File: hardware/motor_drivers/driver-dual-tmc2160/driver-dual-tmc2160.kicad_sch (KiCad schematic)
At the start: 76 parts, among them M1 Micro-Fit 3.0, M2 Micro-Fit 3.0, Q1 DMHT6016LFJ, Q2 DMHT6016LFJ, Q3 DMHT6016LFJ, Q4 DMHT6016LFJ, T1 GND, T10 SCK, T11 GND, T12 DIR, T13 ENCB, T14 SDI, T15 EN, T16 ENCN, T17 SDO, T18 VCC, T19 SPI_MODE, T2 CS0, T20 SD_MODE, T21 Therm, T3 DIAG0, T4 CLK, T5 STEP, T6 DIAG1, T7 12V, T8 GND, T9 ENCA, U1 TMC2160, U2 TMC2160

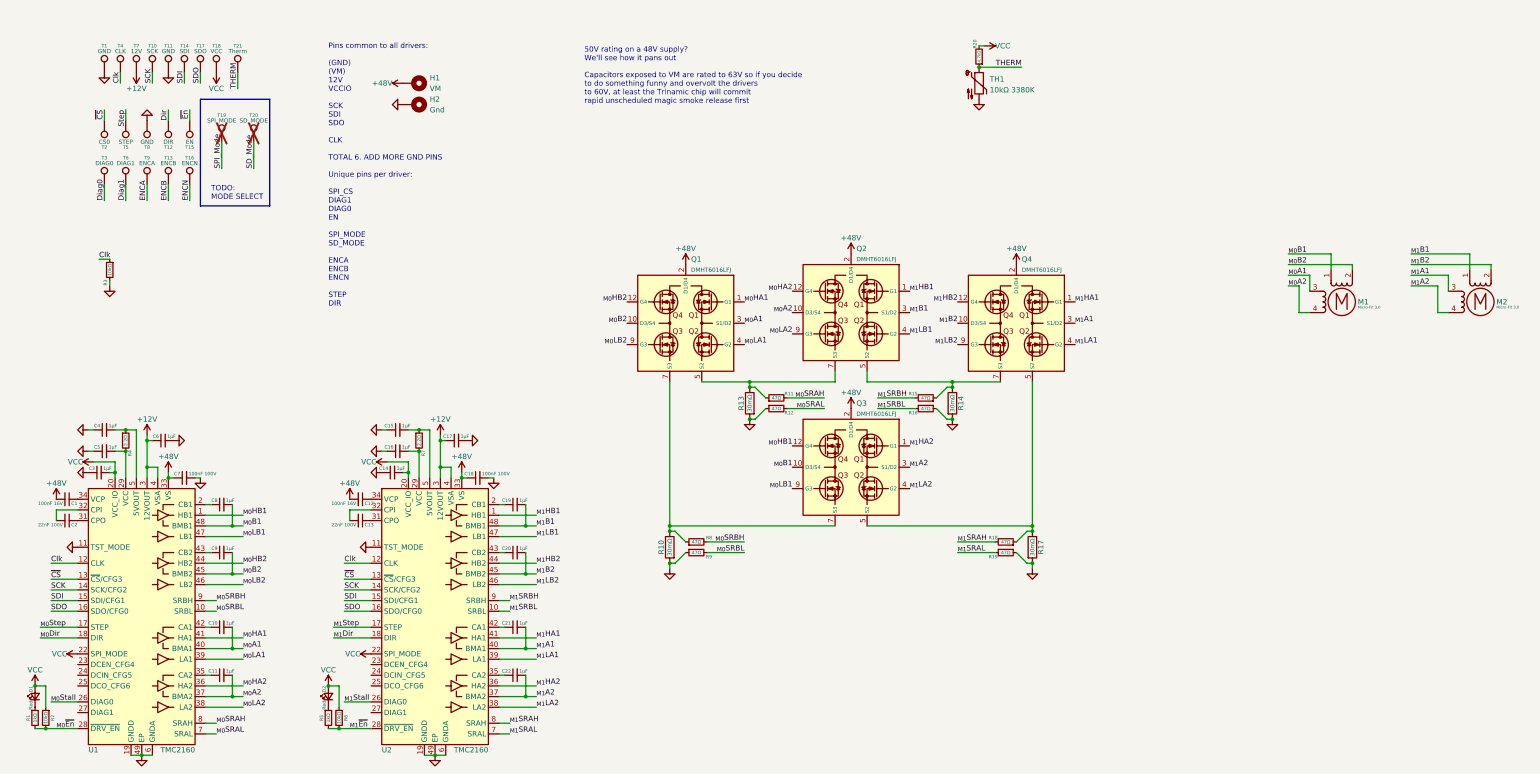
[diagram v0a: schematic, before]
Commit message: added ctb v0.3 and dual 2160, fixed typo in v0.6 manual
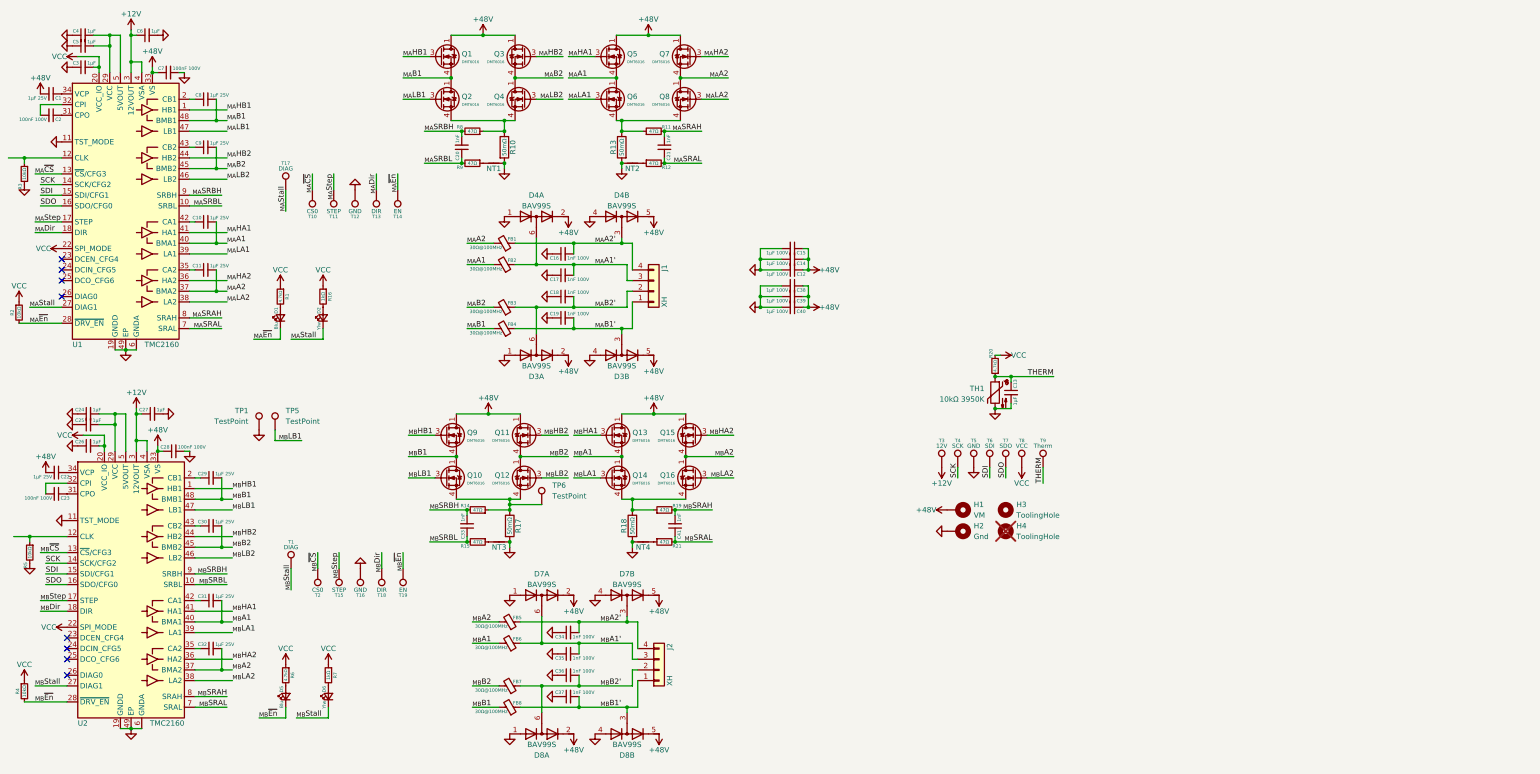
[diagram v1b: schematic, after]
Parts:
- removed M2: Micro-Fit 3.0, corevus:XKB_X3025WR-04, symbol Motor:Stepper_Motor_bipolar
- removed Q1, Q2, Q3, Q4: DMHT6016LFJ, corevus:V-DFN5045-12-Type-B, symbol corevus:DMHT6016LFJ
- removed R14: 30mΩ, Resistor_SMD:R_1206_3216Metric, symbol Device:R
- removed R18: 47Ω, AlphaLib:0402R, symbol Device:R_Small
- removed T13: ENCB, corevus:LGA_Land, symbol Connector:TestPoint
- removed T20: SD_MODE, corevus:LGA_Land, symbol Connector:TestPoint
- removed T4: CLK, corevus:LGA_Land, symbol Connector:TestPoint
- removed T6: DIAG1, corevus:LGA_Land, symbol Connector:TestPoint
- removed T9: ENCA, corevus:LGA_Land, symbol Connector:TestPoint
- added C23, C28: 100nF 100V, PCM_ME_passives:0402C, symbol Device:C_Small
- added C24, C27: 1μF, PCM_ME_passives:0402C, symbol Device:C_Small
- added C25, C26: 1µF, PCM_ME_passives:0402C, symbol Device:C_Small
- added C29, C30, C31, C32: 1μF 25V, PCM_ME_passives:0402C, symbol Device:C_Small
- added C33, C41: 1nF, PCM_ME_passives:0402C, symbol Device:C_Small
- added C34, C35, C36, C37: 1nF 100V, PCM_ME_passives:0402C, symbol Device:C_Small
- added C38, C39, C40: 1μF 100V, Capacitor_SMD:C_1206_3216Metric, symbol Device:C_Small
- added D3, D4, D7, D8: BAV99S, Package_TO_SOT_SMD:SOT-363_SC-70-6, symbol Diode:BAV99S
- added D5: Blu, PCM_ME_passives:0402LED, symbol Device:LED_Small
- added D6: Ylw, PCM_ME_passives:0402LED, symbol Device:LED_Small
- added FB1, FB2, FB3, FB4, FB5, FB6, FB7, FB8: 30Ω@100MHz, Resistor_SMD:R_1206_3216Metric, symbol Device:FerriteBead_Small
- added H3, H4: ToolingHole, corevus:ToolingHole, symbol Mechanical:MountingHole
- added J2: XH, corevus:JST_XH_1x04, symbol Connector_Generic:Conn_01x04
- added NT1, NT2, NT3, NT4: NetTie_2, corevus:NetTie-2_SMD_Pad0.1mm, symbol Device:NetTie_2
- added Q1, Q10, Q11, Q12, Q13, Q14, Q15, Q16, Q2, Q3, Q4, Q5, Q6, Q7, Q8, Q9: DMT6016, corevus:DMT6016LFDF, symbol corevus:DMT6016LFDF-7
- added R14, R21: 47Ω, PCM_ME_passives:0402R, symbol Device:R_Small
- added R18: 50mΩ, Resistor_SMD:R_1206_3216Metric, symbol Device:R
- added T15: STEP, corevus:LGA_Land_2.5mm, symbol Connector:TestPoint
- added T18: DIR, corevus:LGA_Land_2.5mm, symbol Connector:TestPoint
- added T2: CS0, corevus:LGA_Land_2.5mm, symbol Connector:TestPoint
- added TP1, TP5, TP6: TestPoint, TestPoint:TestPoint_Pad_D1.0mm, symbol Connector:TestPoint
- C1: value 100nF 16V -> 1μF 25V; footprint AlphaLib:0402C -> PCM_ME_passives:0402C
- C10, C11, C22, C8, C9: value 1μF -> 1μF 25V; footprint AlphaLib:0402C -> PCM_ME_passives:0402C
- C12: value 100nF 16V -> 1μF 100V; footprint AlphaLib:0402C -> Capacitor_SMD:C_1206_3216Metric
- C13: value 22nF 100V -> 1μF; footprint AlphaLib:0402C -> PCM_ME_passives:0402C
- C14: value 1µF -> 1μF 100V; footprint AlphaLib:0402C -> Capacitor_SMD:C_1206_3216Metric
- C15: value 1μF -> 1μF 100V; footprint AlphaLib:0402C -> Capacitor_SMD:C_1206_3216Metric
- C16: value 1µF -> 1nF 100V; footprint AlphaLib:0402C -> PCM_ME_passives:0402C
- C17, C19: value 1μF -> 1nF 100V; footprint AlphaLib:0402C -> PCM_ME_passives:0402C
- C18: value 100nF 100V -> 1nF 100V; footprint AlphaLib:0402C -> PCM_ME_passives:0402C
- C2: value 22nF 100V -> 100nF 100V; footprint AlphaLib:0402C -> PCM_ME_passives:0402C
- C20, C21: value 1μF -> 1nF; footprint AlphaLib:0402C -> PCM_ME_passives:0402C
- C3, C4, C5, C6, C7: footprint AlphaLib:0402C -> PCM_ME_passives:0402C
- D1: value Red -> Blu; footprint AlphaLib:0603LED -> PCM_ME_passives:0402LED
- D2: value Red -> Ylw; footprint AlphaLib:0603LED -> PCM_ME_passives:0402LED
- H1, H2: now left out of the parts list
- J1: renamed from M1; value Micro-Fit 3.0 -> XH; footprint corevus:XKB_X3025WR-04 -> corevus:JST_XH_1x04; symbol Motor:Stepper_Motor_bipolar -> Connector_Generic:Conn_01x04
- R1: value 1kΩ -> 4.7kΩ; footprint AlphaLib:0402R -> PCM_ME_passives:0402R
- R10, R13, R17: value 30mΩ -> 50mΩ
- R11, R12, R15, R19, R2, R20, R3, R8, R9: footprint AlphaLib:0402R -> PCM_ME_passives:0402R
- R16: value 47Ω -> 1kΩ; footprint AlphaLib:0402R -> PCM_ME_passives:0402R
- R4: value 2.2Ω -> 10kΩ; footprint AlphaLib:0402R -> PCM_ME_passives:0402R
- R5: value 1kΩ -> 10kΩ; footprint AlphaLib:0402R -> PCM_ME_passives:0402R
- R6: value 10kΩ -> 4.7kΩ; footprint AlphaLib:0402R -> PCM_ME_passives:0402R
- R7: value 2.2Ω -> 1kΩ; footprint AlphaLib:0402R -> PCM_ME_passives:0402R
- T1: value GND -> DIAG; footprint corevus:LGA_Land -> corevus:LGA_Land_2.5mm
- T10: renamed from T2; footprint corevus:LGA_Land -> corevus:LGA_Land_2.5mm
- T11: renamed from T5; footprint corevus:LGA_Land -> corevus:LGA_Land_2.5mm
- T12: renamed from T8; footprint corevus:LGA_Land -> corevus:LGA_Land_2.5mm
- T13: renamed from T12; footprint corevus:LGA_Land -> corevus:LGA_Land_2.5mm
- T14: renamed from T15; footprint corevus:LGA_Land -> corevus:LGA_Land_2.5mm
- T16: value ENCN -> GND; footprint corevus:LGA_Land -> corevus:LGA_Land_2.5mm
- T17: renamed from T3; value DIAG0 -> DIAG; footprint corevus:LGA_Land -> corevus:LGA_Land_2.5mm
- T19: value SPI_MODE -> EN; footprint corevus:LGA_Land -> corevus:LGA_Land_2.5mm; now fitted
- T3: renamed from T7; footprint corevus:LGA_Land -> corevus:LGA_Land_2.5mm
- T4: renamed from T10; footprint corevus:LGA_Land -> corevus:LGA_Land_2.5mm
- T5: renamed from T11; footprint corevus:LGA_Land -> corevus:LGA_Land_2.5mm
- T6: renamed from T14; footprint corevus:LGA_Land -> corevus:LGA_Land_2.5mm
- T7: renamed from T17; footprint corevus:LGA_Land -> corevus:LGA_Land_2.5mm
- T8: renamed from T18; footprint corevus:LGA_Land -> corevus:LGA_Land_2.5mm
- T9: renamed from T21; footprint corevus:LGA_Land -> corevus:LGA_Land_2.5mm
- TH1: value 10kΩ 3380K -> 10kΩ 3950K; footprint AlphaLib:0402R -> PCM_ME_passives:0402R
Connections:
- net Diag0 is gone; now on net _{MA}Stall: T17.1
- net ENCN is gone; now on net GND: T16.1
- net _{M0}Dir is gone; now on net _{MA}Dir: U1.18 (DIR)
- net _{M0}Step is gone; now on net _{MA}Step: U1.17 (STEP)
- net ~{En} is gone; now on net _{MA}~{En}: T14.1
- net +12V: now also C27.1; no longer C17.1
- net +48V: now also C12.1, C14.1, C15.1, C22.2, C28.1, C38.1, C39.1, C40.1, D3.2 (K2), D3.5 (K4), D4.2 (K2), D4.5 (K4), D7.2 (K2), D7.5 (K4), D8.2 (K2), D8.5 (K4), Q1.1 (D), Q1.2 (D), Q1.5 (D), Q1.6 (D), Q1.8 (D), Q11.1 (D), Q11.2 (D), Q11.5 (D), Q11.6 (D), Q11.8 (D), Q13.1 (D), Q13.2 (D), Q13.5 (D), Q13.6 (D), Q13.8 (D), Q15.1 (D), Q15.2 (D), Q15.5 (D), Q15.6 (D), Q15.8 (D), Q3.1 (D), Q3.2 (D), Q3.5 (D), Q3.6 (D), Q3.8 (D), Q5.1 (D), Q5.2 (D), Q5.5 (D), Q5.6 (D), Q5.8 (D), Q7.1 (D), Q7.2 (D), Q7.5 (D), Q7.6 (D), Q7.8 (D), Q9.1 (D), Q9.2 (D), Q9.5 (D), Q9.6 (D), Q9.8 (D); no longer C12.2, C18.1
- net GND: now also C12.2, C13.2, C14.2, C15.2, C17.1, C18.1, C19.1, R5.2, C24.1, C25.1, C26.1, C27.2, C28.2, C34.1, C35.1, C36.1, C37.1, C38.2, C39.2, C40.2, D3.1 (A1), D3.4 (A3), D4.1 (A1), D4.4 (A3), D7.1 (A1), D7.4 (A3), D8.1 (A1), D8.4 (A3), NT1.2, NT2.1, NT3.2, NT4.1, R18.2, TP1.1; no longer C14.1, C15.1, C17.2, C18.2, R12.1, R16.1, R19.1, R9.1, T1.1
- net THERM: now also C13.1
- net VCC: now also R1.1, R16.1, R4.1, R7.1, C26.2; no longer C14.2, D1.2 (A), D2.2 (A)
- net at R11.1, R13.1: now also Q6.4 (S), Q6.7 (S), Q8.4 (S), Q8.7 (S)
- net at R10.1, R8.1: now also Q2.4 (S), Q2.7 (S), Q4.4 (S), Q4.7 (S)
- net _{MA}Stall: now reaches U1.27 (DIAG1)
- net _{MA}Stall: now also D2.1 (K)
- net at C5.2, U1.29 (VCC): now also C4.2, U1.5 (5VOUT); no longer R4.2
- net at U2.31 (CPO): now also C23.1; no longer C13.1
- net at U2.32 (CPI): now also C23.2; no longer C13.2
- net at C22.1: now also U2.34 (VCP); no longer U2.35 (CA2)
- net at U2.42 (CA1): now also C31.1; no longer C21.1
- net _{MA}~{En}: now reaches D1.1 (K)
- net _{MA}~{En}: now also R2.2, U1.28 (~{DRV_EN}); no longer R1.1
- net at U2.2 (CB1): now also C29.1; no longer C19.1
- net at R15.1: now also NT3.1
- net at R17.1: now also Q10.4 (S), Q10.7 (S), Q12.4 (S), Q12.7 (S), R14.1, TP6.1
- net _{MB}Stall: now reaches U2.27 (DIAG1)
- net _{MB}Stall: now also T1.1, D6.1 (K)
- net at U2.43 (CB2): now also C30.1; no longer C20.1
- net at R5.1: now also U2.12 (CLK); no longer D2.1 (K)
- net Clk: no longer names the net of R3.1, U1.12 (CLK)
- net Clk: no longer U2.12 (CLK)
- net Dir renamed _{MA}Dir
- net SPI_Mode renamed _{MB}~{En}
- net _{MB}~{En}: now also R4.2, U2.28 (~{DRV_EN}), D5.1 (K)
- net Step renamed _{MA}Step
- net _{M0}A1 renamed _{MA}A1
- net _{MA}A1: now also FB2.2, Q5.4 (S), Q5.7 (S), Q6.1 (D), Q6.2 (D), Q6.5 (D), Q6.6 (D), Q6.8 (D); no longer J1.3
- net _{M0}A2 renamed _{MA}A2
- net _{MA}A2: now also FB1.2, Q7.4 (S), Q7.7 (S), Q8.1 (D), Q8.2 (D), Q8.5 (D), Q8.6 (D), Q8.8 (D); no longer J1.4
- net _{M0}B1 renamed _{MA}B1
- net _{MA}B1: now also FB4.2, Q1.4 (S), Q1.7 (S), Q2.1 (D), Q2.2 (D), Q2.5 (D), Q2.6 (D), Q2.8 (D); no longer J1.1
- net _{M0}B2 renamed _{MA}B2
- net _{MA}B2: now also FB3.2, Q3.4 (S), Q3.7 (S), Q4.1 (D), Q4.2 (D), Q4.5 (D), Q4.6 (D), Q4.8 (D); no longer J1.2 (-)
- net _{M0}HA1 renamed _{MA}HA1
- net _{MA}HA1: now also Q5.3 (G)
- net _{M0}HA2 renamed _{MA}HA2
- net _{MA}HA2: now also Q7.3 (G)
- net _{M0}HB1 renamed _{MA}HB1
- net _{MA}HB1: now also Q1.3 (G)
- net _{M0}HB2 renamed _{MA}HB2
- net _{MA}HB2: now also Q3.3 (G)
- net _{M0}LA1 renamed _{MA}LA1
- net _{MA}LA1: now also Q6.3 (G)
- net _{M0}LA2 renamed _{MA}LA2
- net _{MA}LA2: now also Q8.3 (G)
- net _{M0}LB1 renamed _{MA}LB1
- net _{MA}LB1: now also Q2.3 (G)
- net _{M0}LB2 renamed _{MA}LB2
- net _{MA}LB2: now also Q4.3 (G)
- net _{M0}SRAH renamed _{MA}SRAH
- net _{MA}SRAH: now also C21.2
- net _{M0}SRAL renamed _{MA}SRAL
- net _{MA}SRAL: now also C21.1
- net _{M0}SRBH renamed _{MA}SRBH
- net _{MA}SRBH: now also C20.2
- net _{M0}SRBL renamed _{MA}SRBL
- net _{MA}SRBL: now also C20.1
- net _{M0}Stall: no longer names the net of U1.26 (DIAG0)
- removed net _{M0}~{En}: R1.2, R2.2, U1.28 (~{DRV_EN})
- net _{M1}A1 renamed _{MB}A1
- net _{MB}A1: now also C31.2, FB6.2, Q13.4 (S), Q13.7 (S), Q14.1 (D), Q14.2 (D), Q14.5 (D), Q14.6 (D), Q14.8 (D); no longer C21.2
- net _{M1}A2 renamed _{MB}A2
- net _{MB}A2: now also C32.2, FB5.2, Q15.4 (S), Q15.7 (S), Q16.1 (D), Q16.2 (D), Q16.5 (D), Q16.6 (D), Q16.8 (D); no longer C22.2
- net _{M1}B1 renamed _{MA}B1'
- net _{MA}B1': now also J1.1 (Pin_1), D3.3 (K1A2), FB4.1; no longer U2.48 (BMB1)
- net _{M1}B2 renamed _{MB}B2
- net _{MB}B2: now also C30.2, FB7.2, Q11.4 (S), Q11.7 (S), Q12.1 (D), Q12.2 (D), Q12.5 (D), Q12.6 (D), Q12.8 (D); no longer C20.2
- net _{M1}Dir renamed _{MB}Dir
- net _{MB}Dir: now also T18.1
- net _{M1}HA1 renamed _{MB}HA1
- net _{MB}HA1: now also Q13.3 (G)
- net _{M1}HA2 renamed _{MB}HA2
- net _{MB}HA2: now also Q15.3 (G)
- net _{M1}HB1 renamed _{MB}HB1
- net _{MB}HB1: now also Q9.3 (G)
- net _{M1}HB2 renamed _{MB}HB2
- net _{MB}HB2: now also Q11.3 (G)
- net _{M1}LA1 renamed _{MB}LA1
- net _{MB}LA1: now also Q14.3 (G)
- net _{M1}LA2 renamed _{MB}LA2
- net _{MB}LA2: now also Q16.3 (G)
- net _{M1}LB1 renamed _{MB}LB1
- net _{MB}LB1: now also Q10.3 (G), TP5.1
- net _{M1}LB2 renamed _{MB}LB2
- net _{MB}LB2: now also Q12.3 (G)
- net _{M1}SRAH renamed _{MB}SRAH
- net _{MB}SRAH: now also R19.2, C41.2
- net _{M1}SRAL renamed _{MB}SRAL
- net _{MB}SRAL: now also C41.1, R21.2; no longer R19.2
- net _{M1}SRBH renamed _{MB}SRBH
- net _{MB}SRBH: now also C33.2, R14.2; no longer R15.2
- net _{M1}SRBL: no longer names the net of R16.2
- net _{M1}SRBL: now also D2.2 (A); no longer U2.10 (SRBL)
- net _{M1}Stall: no longer names the net of U2.26 (DIAG0)
- net _{M1}Step renamed _{MB}Step
- net _{MB}Step: now also T15.1
- removed net _{M1}~{En}: R5.2, R6.2, U2.28 (~{DRV_EN})
- net ~{CS} renamed _{MA}~{CS}
- net _{MA}~{CS}: no longer U2.13 (~{CS}/CFG3)
- new net: Q14.4 (S), Q14.7 (S), Q16.4 (S), Q16.7 (S), R18.1, R19.1
- new net: NT2.2, R12.1
- new net: D6.2 (A), R7.2
- new net: D1.2 (A), R1.2
- new net: C24.2, C25.2, U2.29 (VCC), U2.5 (5VOUT)
- new net: D5.2 (A), R6.2
- new net: NT4.2, R21.1
- new net: C32.1, U2.35 (CA2)
- new net: NT1.1, R9.1
- new net _{MA}A1': C17.2, D4.6 (K3A4), FB2.1, J1.3 (Pin_3)
- new net _{MA}A2': C16.2, D4.3 (K1A2), FB1.1, J1.4 (Pin_4)
- new net _{MA}B2': C18.2, D3.6 (K3A4), FB3.1, J1.2 (Pin_2)
- new net _{MB}A1': C35.2, D7.6 (K3A4), FB6.1, J2.3 (Pin_3)
- new net _{MB}A2': C34.2, D7.3 (K1A2), FB5.1, J2.4 (Pin_4)
- new net _{MB}B1: C29.2, FB8.2, Q10.1 (D), Q10.2 (D), Q10.5 (D), Q10.6 (D), Q10.8 (D), Q9.4 (S), Q9.7 (S), U2.48 (BMB1)
- new net _{MB}B1': C37.2, D8.3 (K1A2), FB8.1, J2.1 (Pin_1)
- new net _{MB}B2': C36.2, D8.6 (K3A4), FB7.1, J2.2 (Pin_2)
- new net _{MB}SRBL: C33.1, R15.2, U2.10 (SRBL)
- new net _{MB}~{CS}: T2.1, U2.13 (~{CS}/CFG3)
- no-connect marks 0 -> 8
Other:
- note removed: "50V rating on a 48V supply? We'll see how it pans out"
- note removed: "Capacitors exposed to VM are rated to 63V so if you decide to do something funny and overvolt the drivers to 60V, at least the Trinamic chip will commit rapid unscheduled magic smoke release first"
- note removed: "Pins common to all drivers: (GND) (VM) 12V VCCIO SCK SDI SDO CLK TOTAL 6. ADD MORE GND PINS Unique pins per driver: SPI_CS DIAG1 DIAG0 EN SPI_MODE SD_MODE ENCA ENCB ENCN STEP DIR"
- note removed: "TODO: MODE SELECT"
- company: (none) -> meridi engineering
- title: (none) -> TMC2160 Stepper Driver Module
- moved on the sheet: C1, C10, C11, C2, C3, C4, C5, C6, C7, C8, C9, H1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

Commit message: last before i go on v0.7
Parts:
- D1, D5: value Blu -> Grn
- H3: now not fitted
- H4: now fitted
- T1, T10, T11, T12, T13, T14, T15, T16, T17, T18, T19, T2, T3, T4, T5, T6, T7, T8, T9, TP1, TP5, TP6: now left out of the parts list
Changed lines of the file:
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@@
 		(mirror x)
 		(unit 1)
-		(exclude_from_sim no)
-		(in_bom yes)
+		(exclude_from_sim yes)
+		(in_bom no)
 		(on_board yes)
 		(dnp no)
@@
 		(mirror x)
 		(unit 1)
-		(exclude_from_sim no)
-		(in_bom yes)
+		(exclude_from_sim yes)
+		(in_bom no)
 		(on_board yes)
 		(dnp no)
@@
 		(mirror x)
 		(unit 1)
-		(exclude_from_sim no)
-		(in_bom yes)
+		(exclude_from_sim yes)
+		(in_bom no)
 		(on_board yes)
 		(dnp no)
@@
 		(mirror x)
 		(unit 1)
-		(exclude_from_sim no)
-		(in_bom yes)
+		(exclude_from_sim yes)
+		(in_bom no)
 		(on_board yes)
 		(dnp no)
@@
 		(mirror x)
 		(unit 1)
-		(exclude_from_sim no)
-		(in_bom yes)
+		(exclude_from_sim yes)
+		(in_bom no)
 		(on_board yes)
 		(dnp no)
@@
 		(at 140.97 130.81 0)
 		(unit 1)
-		(exclude_from_sim no)
-		(in_bom yes)
+		(exclude_from_sim yes)
+		(in_bom no)
 		(on_board yes)
 		(dnp no)
@@
 			)
 		)
-		(property "Value" "Blu"
+		(property "Value" "Grn"
 			(at 79.01 177.53 0)
 			(effects
@@
 		(at 80.01 55.88 0)
 		(unit 1)
-		(exclude_from_sim no)
-		(in_bom yes)
+		(exclude_from_sim yes)
+		(in_bom no)
 		(on_board yes)
 		(dnp no)
@@
 		(at 251.46 121.92 0)
 		(unit 1)
-		(exclude_from_sim no)
-		(in_bom yes)
+		(exclude_from_sim yes)
+		(in_bom no)
 		(on_board yes)
 		(dnp no)
@@
 		(at 236.22 121.92 0)
 		(unit 1)
-		(exclude_from_sim no)
-		(in_bom yes)
+		(exclude_from_sim yes)
+		(in_bom no)
 		(on_board yes)
 		(dnp no)
@@
 		(mirror x)
 		(unit 1)
-		(exclude_from_sim no)
-		(in_bom yes)
+		(exclude_from_sim yes)
+		(in_bom no)
 		(on_board yes)
 		(dnp no)
@@
 		(mirror y)
 		(unit 1)
-		(exclude_from_sim no)
-		(in_bom yes)
+		(exclude_from_sim yes)
+		(in_bom no)
 		(on_board yes)
 		(dnp no)
@@
 			)
 		)
-		(property "Value" "Blu"
+		(property "Value" "Grn"
 			(at 77.74 87.36 0)
 			(effects
@@
 		(at 86.36 55.88 180)
 		(unit 1)
-		(exclude_from_sim no)
-		(in_bom yes)
+		(exclude_from_sim yes)
+		(in_bom no)
 		(on_board yes)
 		(dnp no)
@@
 		(exclude_from_sim no)
 		(in_bom no)
-		(on_board no)
-		(dnp yes)
+		(on_board yes)
+		(dnp no)
 		(fields_autoplaced yes)
 		(property "Reference" "H4"
@@
 		(mirror x)
 		(unit 1)
-		(exclude_from_sim no)
-		(in_bom yes)
+		(exclude_from_sim yes)
+		(in_bom no)
 		(on_board yes)
 		(dnp no)
@@
 		(exclude_from_sim no)
 		(in_bom no)
-		(on_board yes)
-		(dnp no)
+		(on_board no)
+		(dnp yes)
 		(fields_autoplaced yes)
 		(property "Reference" "H3"
@@
 		(at 81.28 146.05 0)
 		(unit 1)
-		(exclude_from_sim no)
-		(in_bom yes)
+		(exclude_from_sim yes)
+		(in_bom no)
 		(on_board yes)
 		(dnp no)
@@
 		(at 260.35 121.92 0)
 		(unit 1)
-		(exclude_from_sim no)
-		(in_bom yes)
+		(exclude_from_sim yes)
+		(in_bom no)
 		(on_board yes)
 		(dnp no)
@@
 		(mirror x)
 		(unit 1)
-		(exclude_from_sim no)
-		(in_bom yes)
+		(exclude_from_sim yes)
+		(in_bom no)
 		(on_board yes)
 		(dnp no)
@@
 		(at 77.47 113.03 0)
 		(unit 1)
-		(exclude_from_sim no)
-		(in_bom yes)
+		(exclude_from_sim yes)
+		(in_bom no)
 		(on_board yes)
 		(dnp no)
@@
 		(at 247.65 121.92 0)
 		(unit 1)
-		(exclude_from_sim no)
-		(in_bom yes)
+		(exclude_from_sim yes)
+		(in_bom no)
 		(on_board yes)
 		(dnp no)
@@
 		(at 87.63 146.05 180)
 		(unit 1)
-		(exclude_from_sim no)
-		(in_bom yes)
+		(exclude_from_sim yes)
+		(in_bom no)
 		(on_board yes)
 		(dnp no)
@@
 		(at 255.27 121.92 0)
 		(unit 1)
-		(exclude_from_sim no)
-		(in_bom yes)
+		(exclude_from_sim yes)
+		(in_bom no)
 		(on_board yes)
 		(dnp no)
@@
 		(at 240.03 121.92 0)
 		(unit 1)
-		(exclude_from_sim no)
-		(in_bom yes)
+		(exclude_from_sim yes)
+		(in_bom no)
 		(on_board yes)
 		(dnp no)
@@
 		(at 243.84 121.92 0)
 		(unit 1)
-		(exclude_from_sim no)
-		(in_bom yes)
+		(exclude_from_sim yes)
+		(in_bom no)
 		(on_board yes)
 		(dnp no)

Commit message: update toolboard, change documentation
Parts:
- added C42, C43, C44, C45, C46, C47, C48, C49, C50: 100nF 100V, PCM_ME_passives:0402C, symbol Device:C_Small
- added FID1, FID2, FID3, FID4: Fiducial, Fiducial:Fiducial_0.5mm_Mask1mm, symbol Mechanical:Fiducial
- added NT5, NT6, NT7, NT8: NetTie_2, corevus:NetTie-2_SMD_Pad0.15mm, symbol Device:NetTie_2
- C20, C21, C33, C41: value 1nF -> 1nF
- D1, D2, D5, D6: footprint PCM_ME_passives:0402LED -> PCM_ME_passives:0603LED
- H4, TP6: now not fitted
- NT1, NT2, NT3, NT4: footprint corevus:NetTie-2_SMD_Pad0.1mm -> corevus:NetTie-2_SMD_Pad0.15mm
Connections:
- net +48V: now also C42.1, C43.1, C44.1, C45.1, C46.1, C47.1, C48.1, C49.1, C50.1
- net GND: now also NT2.2, C42.2, C43.2, C44.2, C45.2, C46.2, C47.2, C48.2, C49.2, C50.2, NT6.2, NT8.1; no longer NT1.2, NT2.1, NT3.2
- net at Q6.4 (S), Q6.7 (S), Q8.4 (S)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: now also NT3.1; no longer R11.1
- net at Q14.4 (S), Q14.7 (S), Q16.4 (S)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: now also NT7.1; no longer R19.1
- net at Q10.4 (S), Q10.7 (S), Q12.4 (S)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: now also NT5.2; no longer R14.1
- net at R12.1: now also NT4.2; no longer NT2.2
- net at Q2.4 (S), Q2.7 (S), Q4.4 (S)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: now also NT1.2; no longer R8.1
- net at R21.1: now also NT8.2; no longer NT4.2
- net at R15.1: now also NT6.1; no longer NT3.1
- net at NT1.1: now also R8.1; no longer R9.1
- new net: NT3.2, R11.1
- new net: NT7.2, R19.1
- new net: NT2.1, R9.1
- new net: NT5.1, R14.1
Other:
- moved on the sheet: C22, C23
